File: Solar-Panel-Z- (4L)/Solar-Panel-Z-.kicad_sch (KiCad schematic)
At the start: 73 parts, among them J1 FTS-105-01-L-DV-A, Q1 BSS138DWQ-7, Q2 MBT2222ADW1T1, Q3 BSS138DWQ-7, Q4 MBT2222ADW1T1, U1 BQ25570RGRR, U2 TSL2561

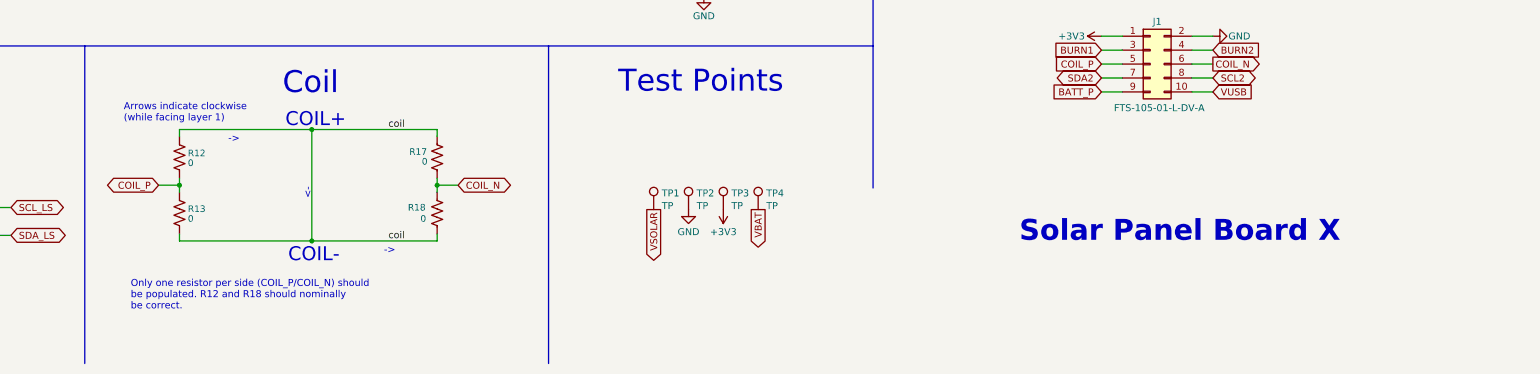
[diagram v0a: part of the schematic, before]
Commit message: Added 4 Layer Z+ board
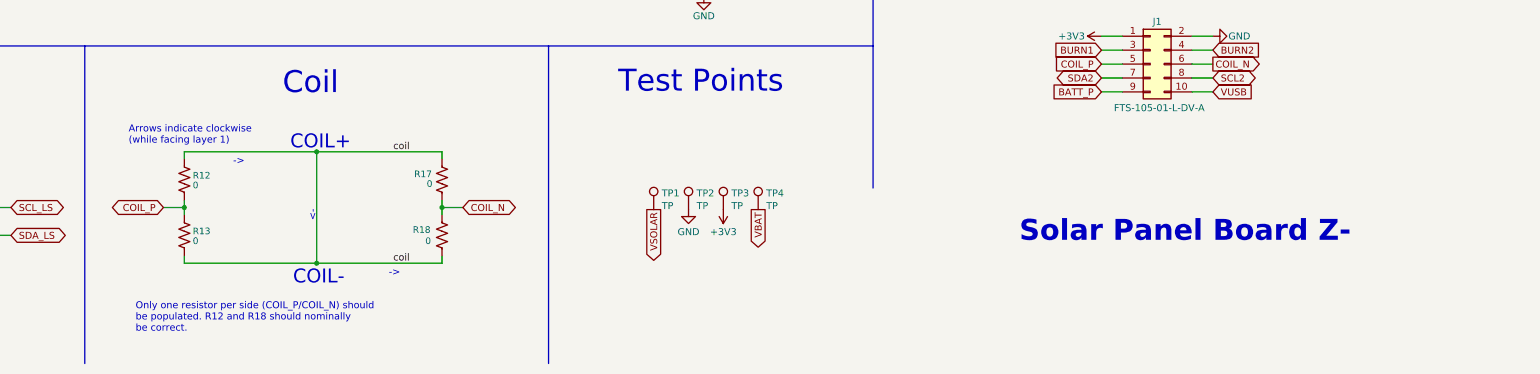
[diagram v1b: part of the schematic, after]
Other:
- note added: "Solar Panel Board Z-"
- note removed: "Solar Panel Board X"
- moved on the sheet: R12, R13, R17, R18

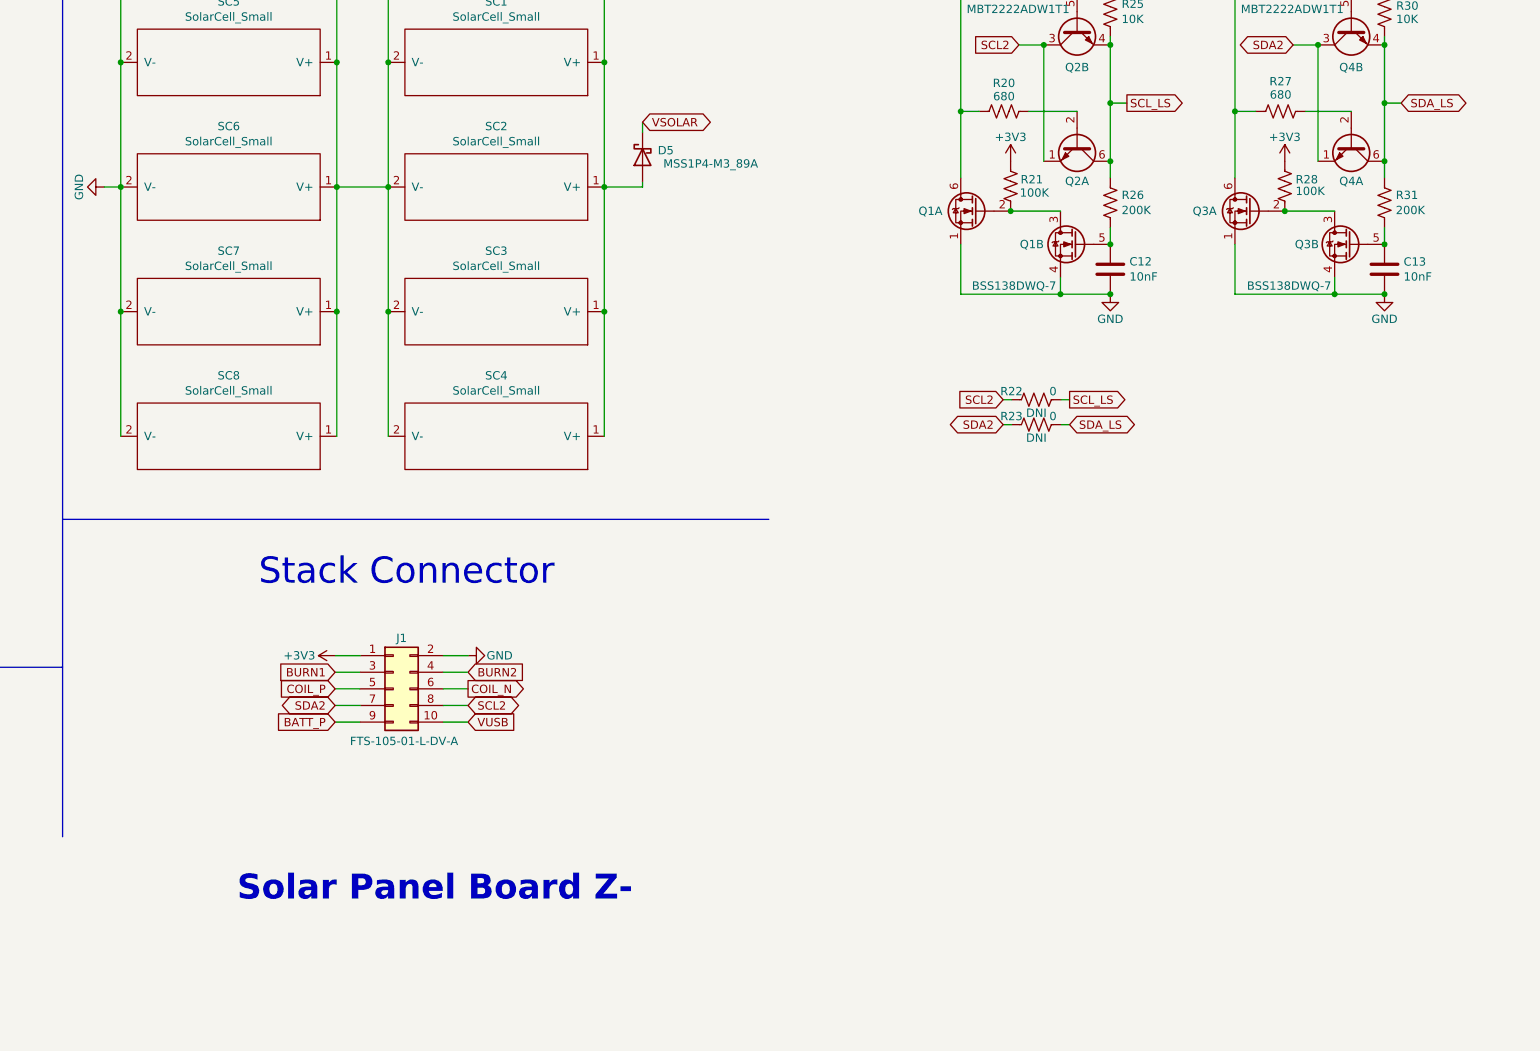
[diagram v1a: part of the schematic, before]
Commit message: Added 4 Layer Z- board
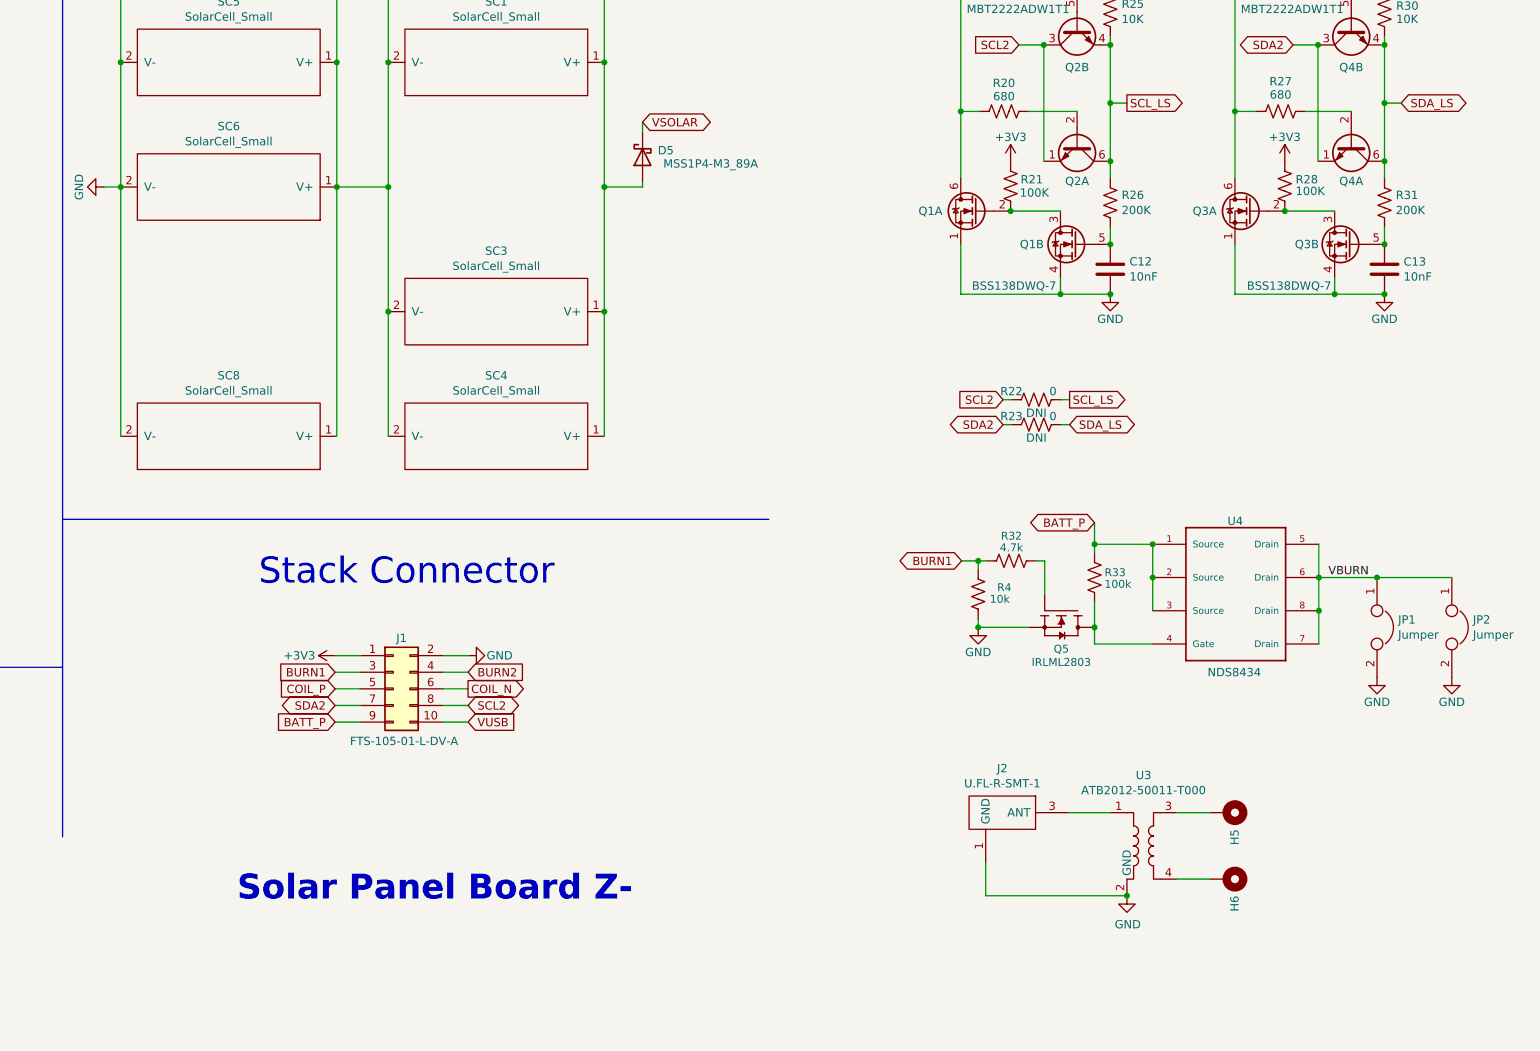
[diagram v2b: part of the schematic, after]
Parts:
- removed SC2, SC7: SolarCell_Small, solarpanels:KXOB25-05X3F, symbol solarpanels:SolarCell_Small
- added H5, H6: MountingHole_Pad, solarpanels:Antenna Pad, symbol Mechanical:MountingHole_Pad
- added J2: U.FL-R-SMT-1, solarpanels:U.FL-R-SMT-1, symbol solarpanels:U.FL-R-SMT-1
- added JP1, JP2: Jumper, solarpanels:Burn-Wire-Rotated, symbol solarpanels:Device_Jumper
- added Q5: IRLML2803, Package_TO_SOT_SMD:SOT-23, symbol solarpanels:IRLML2803TRPBF
- added R32: 4.7k, Resistor_SMD:R_0603_1608Metric, symbol Device:R_US
- added R33: 100k, Resistor_SMD:R_0603_1608Metric, symbol Device:R_US
- added R4: 10k, Resistor_SMD:R_0603_1608Metric, symbol Device:R_US
- added U3: ATB2012-50011-T000, solarpanels:ATB2012, symbol solarpanels:ATB2012
- added U4: NDS8434, solarpanels:NDS8434, symbol solarpanels:symbols_NDS8434
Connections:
- net BATT_P: now also R33.2, U4.1 (Source), U4.2 (Source), U4.3 (Source)
- net BURN1: now also R32.2, R4.1
- net GND: now also J2.1 (GND), J2.2, JP1.2, JP2.2, Q5.2 (S), R4.2, U3.2 (GND)
- new net: H5.1, U3.3
- new net: J2.3 (ANT), U3.1
- new net: H6.1, U3.4
- new net: Q5.1 (G), R32.1
- new net: Q5.3 (D), R33.1, U4.4 (Gate)
- new net VBURN: JP1.1, JP2.1, U4.5 (Drain), U4.6 (Drain), U4.7 (Drain), U4.8 (Drain)

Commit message: Z board updates
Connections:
- net SCL2 renamed SCL
- net SDA2 renamed SDA
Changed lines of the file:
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@@
     )
   )
-  (global_label "SCL2" (shape input) (at 381.889 50.927 180) (fields_autoplaced)
+  (global_label "SCL" (shape input) (at 381.889 50.927 180) (fields_autoplaced)
     (effects (font (size 1.27 1.27)) (justify right))
-    (property "Intersheet References" "${INTERSHEET_REFS}" (id 0) (at 374.8477 50.8476 0)
+    (property "Intersheet References" "${INTERSHEET_REFS}" (id 0) (at 376.0572 50.8476 0)
       (effects (font (size 1.27 1.27)) (justify right) hide)
     )
@@
     )
   )
-  (global_label "SCL2" (shape input) (at 379.476 105.156 180) (fields_autoplaced)
+  (global_label "SCL" (shape input) (at 379.476 105.156 180) (fields_autoplaced)
     (effects (font (size 1.27 1.27)) (justify right))
-    (property "Intersheet References" "${INTERSHEET_REFS}" (id 0) (at 372.4347 105.0766 0)
+    (property "Intersheet References" "${INTERSHEET_REFS}" (id 0) (at 373.6442 105.0766 0)
       (effects (font (size 1.27 1.27)) (justify right) hide)
     )
@@
     )
   )
-  (global_label "BURN1" (shape input) (at 277.368 146.812 180) (fields_autoplaced)
+  (global_label "BURN1" (shape output) (at 277.368 146.812 180) (fields_autoplaced)
     (effects (font (size 1.27 1.27)) (justify right))
-    (property "Intersheet References" "${INTERSHEET_REFS}" (id 0) (at 85.598 -83.058 0)
-      (effects (font (size 1.27 1.27)) hide)
+    (property "Intersheet References" "${INTERSHEET_REFS}" (id 0) (at 268.6333 146.7326 0)
+      (effects (font (size 1.27 1.27)) (justify right) hide)
     )
   )
-  (global_label "COIL_N" (shape output) (at 297.688 149.352 0) (fields_autoplaced)
+  (global_label "COIL_N" (shape input) (at 297.688 149.352 0) (fields_autoplaced)
     (effects (font (size 1.27 1.27)) (justify left))
     (property "Intersheet References" "${INTERSHEET_REFS}" (id 0) (at 306.5436 149.2726 0)
@@
     )
   )
-  (global_label "BURN2" (shape input) (at 297.688 146.812 0) (fields_autoplaced)
+  (global_label "BURN2" (shape output) (at 297.688 146.812 0) (fields_autoplaced)
     (effects (font (size 1.27 1.27)) (justify left))
-    (property "Intersheet References" "${INTERSHEET_REFS}" (id 0) (at 83.058 -83.058 0)
-      (effects (font (size 1.27 1.27)) hide)
+    (property "Intersheet References" "${INTERSHEET_REFS}" (id 0) (at 306.4227 146.7326 0)
+      (effects (font (size 1.27 1.27)) (justify left) hide)
     )
   )
@@
     )
   )
-  (global_label "SDA2" (shape bidirectional) (at 379.476 108.966 180) (fields_autoplaced)
+  (global_label "SDA" (shape bidirectional) (at 379.476 108.966 180) (fields_autoplaced)
     (effects (font (size 1.27 1.27)) (justify right))
-    (property "Intersheet References" "${INTERSHEET_REFS}" (id 0) (at 372.3742 108.8866 0)
+    (property "Intersheet References" "${INTERSHEET_REFS}" (id 0) (at 373.5837 108.8866 0)
       (effects (font (size 1.27 1.27)) (justify right) hide)
     )
@@
     )
   )
-  (global_label "SCL2" (shape bidirectional) (at 297.688 151.892 0) (fields_autoplaced)
+  (global_label "SCL" (shape output) (at 297.688 151.892 0) (fields_autoplaced)
     (effects (font (size 1.27 1.27)) (justify left))
-    (property "Intersheet References" "${INTERSHEET_REFS}" (id 0) (at 304.7293 151.8126 0)
+    (property "Intersheet References" "${INTERSHEET_REFS}" (id 0) (at 303.5198 151.8126 0)
       (effects (font (size 1.27 1.27)) (justify left) hide)
     )
   )
-  (global_label "COIL_P" (shape input) (at 277.368 149.352 180) (fields_autoplaced)
+  (global_label "COIL_P" (shape output) (at 277.368 149.352 180) (fields_autoplaced)
     (effects (font (size 1.27 1.27)) (justify right))
     (property "Intersheet References" "${INTERSHEET_REFS}" (id 0) (at 268.5728 149.2726 0)
@@
     )
   )
-  (global_label "BATT_P" (shape input) (at 277.368 154.432 180) (fields_autoplaced)
+  (global_label "BATT_P" (shape output) (at 277.368 154.432 180) (fields_autoplaced)
     (effects (font (size 1.27 1.27)) (justify right))
     (property "Intersheet References" "${INTERSHEET_REFS}" (id 0) (at 268.5124 154.3526 0)
@@
     )
   )
-  (global_label "VUSB" (shape input) (at 297.688 154.432 0) (fields_autoplaced)
+  (global_label "VUSB" (shape output) (at 297.688 154.432 0) (fields_autoplaced)
     (effects (font (size 1.27 1.27)) (justify left))
     (property "Intersheet References" "${INTERSHEET_REFS}" (id 0) (at 304.9108 154.3526 0)
@@
     )
   )
-  (global_label "SDA2" (shape bidirectional) (at 423.799 50.927 180) (fields_autoplaced)
+  (global_label "SDA" (shape bidirectional) (at 423.799 50.927 180) (fields_autoplaced)
     (effects (font (size 1.27 1.27)) (justify right))
-    (property "Intersheet References" "${INTERSHEET_REFS}" (id 0) (at 416.6972 50.8476 0)
+    (property "Intersheet References" "${INTERSHEET_REFS}" (id 0) (at 417.9067 50.8476 0)
       (effects (font (size 1.27 1.27)) (justify right) hide)
     )
@@
     )
   )
-  (global_label "SDA2" (shape bidirectional) (at 277.368 151.892 180) (fields_autoplaced)
+  (global_label "SDA" (shape bidirectional) (at 277.368 151.892 180) (fields_autoplaced)
     (effects (font (size 1.27 1.27)) (justify right))
-    (property "Intersheet References" "${INTERSHEET_REFS}" (id 0) (at 270.2662 151.8126 0)
+    (property "Intersheet References" "${INTERSHEET_REFS}" (id 0) (at 271.4757 151.8126 0)
       (effects (font (size 1.27 1.27)) (justify right) hide)
     )
